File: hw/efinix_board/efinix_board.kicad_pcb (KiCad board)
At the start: 4 copper layers, 62.2 x 56.9 mm, 55 parts, among them U1 T20F256, U2 TPS62826, U3 TPS62826

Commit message: Start working on sdram
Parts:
- added C43: 4.7u, Capacitor_SMD:C_0402_1005Metric, F.Cu at (117.6, 33.2)
- added C44: 0.1u, Capacitor_SMD:C_0201_Small, F.Cu at (105.0, 31.4)
- added C45: 0.1u, Capacitor_SMD:C_0201_Small, F.Cu at (92.0, 33.2)
- added C46: 0.1u, Capacitor_SMD:C_0201_Small, F.Cu at (117.6, 34.2)
- added C47: 4.7u, Capacitor_SMD:C_0402_1005Metric, F.Cu at (117.6, 36.4)
- added C48: 0.1u, Capacitor_SMD:C_0201_Small, F.Cu at (111.8, 46.6)
- added C49: 0.1u, Capacitor_SMD:C_0201_Small, F.Cu at (109.4, 31.4)
- added C50: 0.1u, Capacitor_SMD:C_0201_Small, F.Cu at (113.3, 31.4)
- added C51: 0.1u, Capacitor_SMD:C_0201_Small, F.Cu at (107.0, 46.6)
- added L4: 33 @100MHz, Inductor_SMD:L_0402_1005Metric, F.Cu at (117.6, 35.2)
- added U4: NDS36PT5, Package_SO:TSOP-II-54_22.2x10.16mm_P0.8mm, F.Cu at (104.2, 39.0)
- moved C41 9.18 mm to (67.8, 33.5)
- moved R2 9.18 mm to (74.8, 31.2)
- moved U2 9.18 mm to (77.6, 31.2)
- moved U3 9.18 mm to (66.0, 31.2)
- moved C40 9.18 mm to (62.3, 33.2)
- moved R6 9.18 mm to (63.3, 33.2)
- moved R7 9.18 mm to (64.3, 33.2)
- moved R5 9.18 mm to (63.2, 31.2)
- moved C38 9.18 mm to (79.4, 33.5)
- moved C39 9.18 mm to (79.5, 31.2)
- moved C42 9.18 mm to (67.9, 31.2)
- moved C37 9.18 mm to (73.9, 33.2)
- moved L2 9.18 mm to (82.8, 32.6)
- moved L3 9.18 mm to (71.2, 32.6)
- moved R3 9.18 mm to (74.9, 33.2)
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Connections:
- U1 pad A11: unconnected-(U1-PadA11) -> /fpga/DQ6
- U1 pad A13: unconnected-(U1-PadA13) -> /fpga/DQ3
- U1 pad A14: unconnected-(U1-PadA14) -> /fpga/DQ1
- U1 pad A15: unconnected-(U1-PadA15) -> /fpga/DQ15
- U1 pad B10: unconnected-(U1-PadB10) -> /fpga/DQ7
- U1 pad B11: unconnected-(U1-PadB11) -> /fpga/DQ5
- U1 pad B12: unconnected-(U1-PadB12) -> /fpga/DQ4
- U1 pad B13: unconnected-(U1-PadB13) -> /fpga/DQ2
- U1 pad B14: unconnected-(U1-PadB14) -> /fpga/DQ0
- U1 pad B15: unconnected-(U1-PadB15) -> /fpga/DQ14
- U1 pad B16: unconnected-(U1-PadB16) -> /fpga/DQ13
- U1 pad B9: unconnected-(U1-PadB9) -> /fpga/LQDM
- U1 pad C11: unconnected-(U1-PadC11) -> /fpga/A2
- U1 pad C12: unconnected-(U1-PadC12) -> /fpga/A0
- U1 pad C13: unconnected-(U1-PadC13) -> /fpga/BA1
- U1 pad C14: unconnected-(U1-PadC14) -> /fpga/BA0
- U1 pad C15: unconnected-(U1-PadC15) -> /fpga/DQ12
- U1 pad C16: unconnected-(U1-PadC16) -> /fpga/Q11
- U1 pad D11: unconnected-(U1-PadD11) -> /fpga/A1
- U1 pad D12: unconnected-(U1-PadD12) -> /fpga/A10
- U1 pad D13: unconnected-(U1-PadD13) -> /fpga/~{CS}
- U1 pad D16: unconnected-(U1-PadD16) -> /fpga/DQ10
- U1 pad E11: unconnected-(U1-PadE11) -> /fpga/A3
- U1 pad E12: unconnected-(U1-PadE12) -> /fpga/~{RAS}
- U1 pad E16: unconnected-(U1-PadE16) -> /fpga/DQ9
- U1 pad H12: unconnected-(U1-PadH12) -> /fpga/~{CAS}
- U1 pad J12: unconnected-(U1-PadJ12) -> /fpga/~{WE}
- U1 pad J13: unconnected-(U1-PadJ13) -> /fpga/A4
- U1 pad J14: unconnected-(U1-PadJ14) -> /fpga/A5
- U1 pad J15: unconnected-(U1-PadJ15) -> /fpga/A6
- U1 pad K12: unconnected-(U1-PadK12) -> /fpga/A7
- U1 pad K14: unconnected-(U1-PadK14) -> /fpga/A8
- U1 pad K15: unconnected-(U1-PadK15) -> /fpga/DQ8
- U1 pad K16: unconnected-(U1-PadK16) -> /fpga/UQDM
- U1 pad L15: unconnected-(U1-PadL15) -> /fpga/A9
- U1 pad L16: unconnected-(U1-PadL16) -> /fpga/A11
- U1 pad M15: unconnected-(U1-PadM15) -> /fpga/A12
- U1 pad M16: unconnected-(U1-PadM16) -> /fpga/~{CKE}
- U1 pad P16: unconnected-(U1-PadP16) -> /fpga/CLK
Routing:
- net /fpga/~{WE}: track 0.00 -> 32.1 mm, vias 0 -> 2
- net /fpga/~{CAS}: track 0.00 -> 31.6 mm, vias 0 -> 2
- net /fpga/~{RAS}: track 0.00 -> 27.9 mm, vias 0 -> 2
- net /fpga/~{CS}: track 0.00 -> 25.9 mm, vias 0 -> 2
- net /fpga/A10: track 0.00 -> 24.4 mm, vias 0 -> 2
- net /fpga/A2: track 0.00 -> 24.3 mm, vias 0 -> 2
- net /fpga/A3: track 0.00 -> 24.1 mm, vias 0 -> 2
- net /fpga/A6: track 0.00 -> 24.0 mm, vias 0 -> 2
- net /fpga/BA0: track 0.00 -> 23.8 mm, vias 0 -> 2
- net /fpga/A1: track 0.00 -> 23.8 mm, vias 0 -> 2
- net /fpga/BA1: track 0.00 -> 23.7 mm, vias 0 -> 2
- net /fpga/A4: track 0.00 -> 23.7 mm, vias 0 -> 2
- net /fpga/A7: track 0.00 -> 23.6 mm, vias 0 -> 2
- net /fpga/A5: track 0.00 -> 23.6 mm, vias 0 -> 2
- net /fpga/A8: track 0.00 -> 23.5 mm, vias 0 -> 2
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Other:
- copper layers 4 -> 6

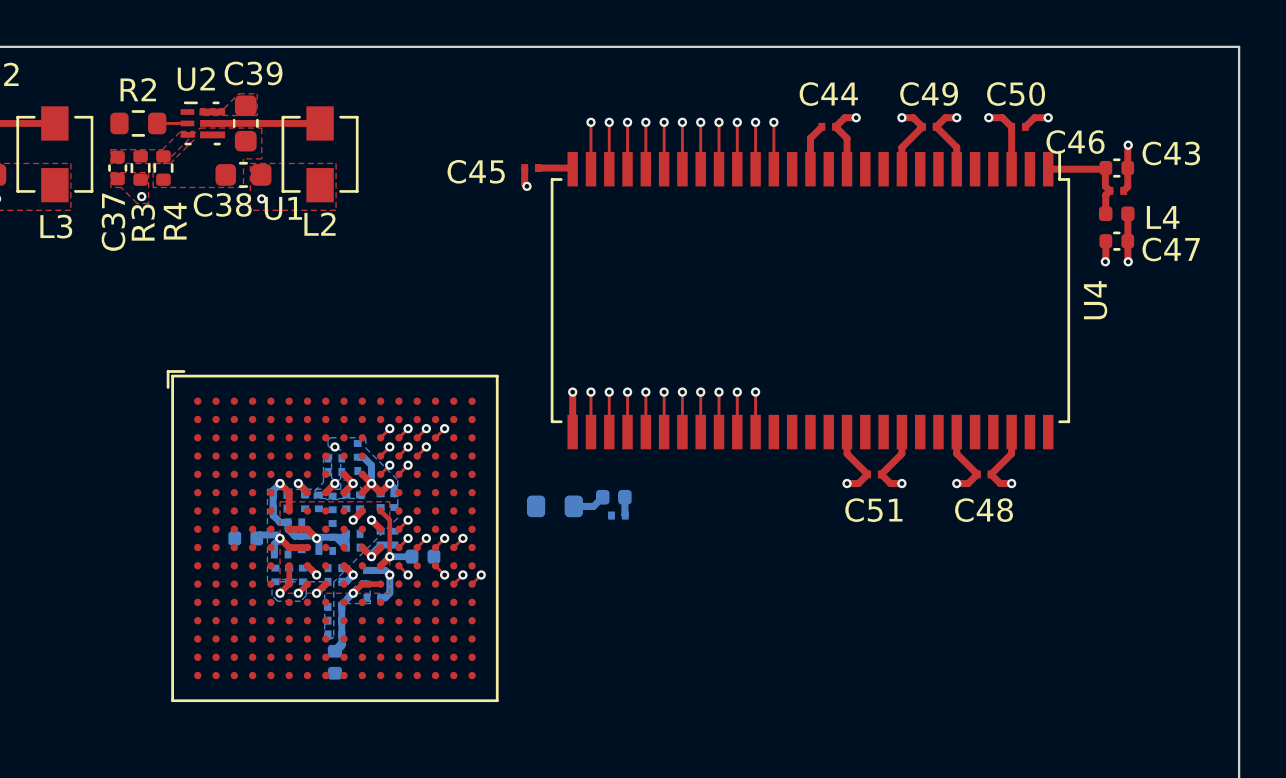
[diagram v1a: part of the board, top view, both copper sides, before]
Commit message: More sdram routing
This changes the pinout from the development board, now DQ8 and UDQM are
different.
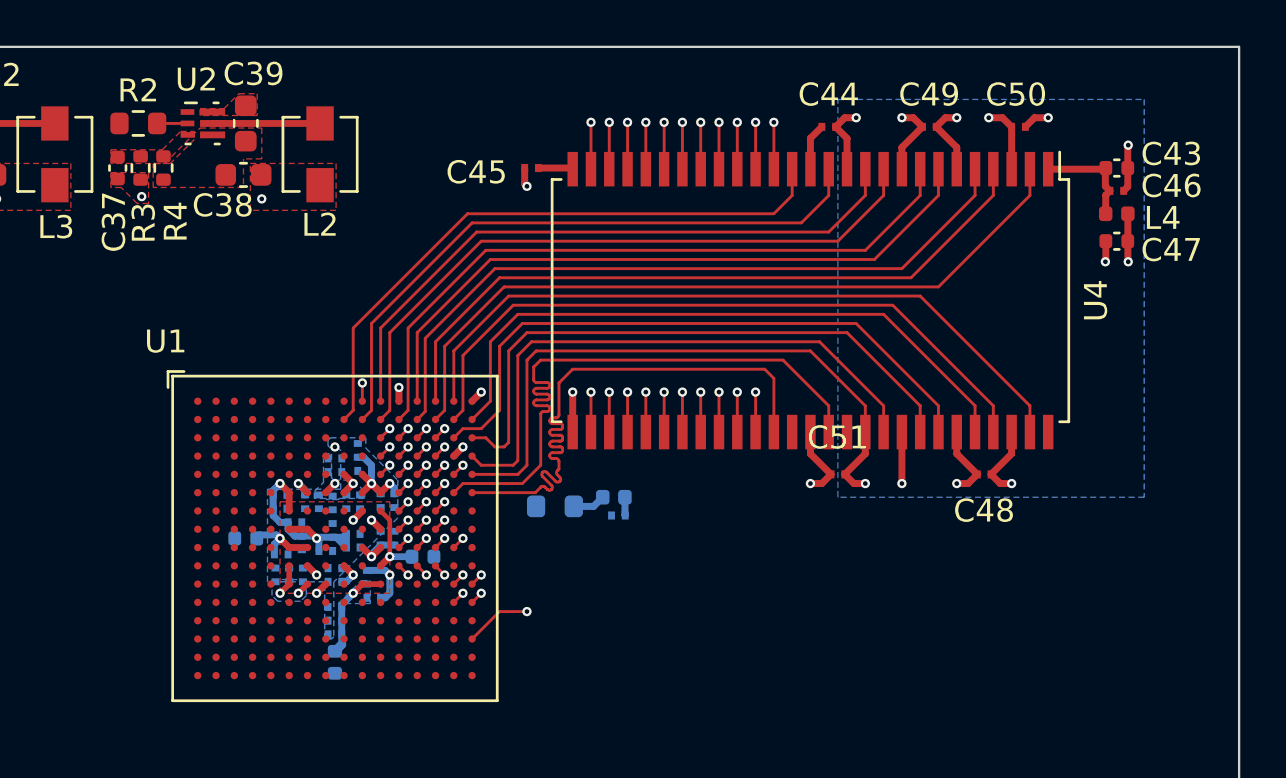
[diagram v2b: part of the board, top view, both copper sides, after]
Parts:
- moved C51 1.60 mm to (105.4, 46.6), turned to 180 degrees
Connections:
- U1 pad C16: /fpga/Q11 -> /fpga/DQ11
- U1 pad F15: unconnected-(U1-PadF15) -> /fpga/DQ8
- U1 pad F16: unconnected-(U1-PadF16) -> /fpga/UQDM
- U1 pad K15: /fpga/DQ8 -> unconnected-(U1-PadK15)
- U1 pad K16: /fpga/UQDM -> unconnected-(U1-PadK16)
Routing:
- net /fpga/DQ0: track 0.00 -> 32.8 mm
- net /fpga/DQ15: track 0.00 -> 31.5 mm
- net /fpga/DQ2: track 0.00 -> 31.5 mm
- net /fpga/DQ1: track 0.00 -> 30.8 mm
- net /fpga/DQ4: track 0.00 -> 30.1 mm
- net /fpga/DQ14: track 0.00 -> 30.0 mm
- net /fpga/DQ3: track 0.00 -> 29.4 mm
- net /fpga/DQ5: track 0.00 -> 29.2 mm
- net /fpga/DQ13: track 0.00 -> 28.2 mm
- net /fpga/DQ6: track 0.00 -> 28.0 mm
- net /fpga/DQ7: track 0.00 -> 27.8 mm
- net /fpga/DQ9: track 0.00 -> 27.6 mm, vias 0 -> 1
- net /fpga/DQ12: track 0.00 -> 27.6 mm
- net /fpga/LQDM: track 0.00 -> 26.9 mm
- net /fpga/DQ8: track 0.00 -> 26.9 mm
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- added copper zone on B.Cu, net VCCQ

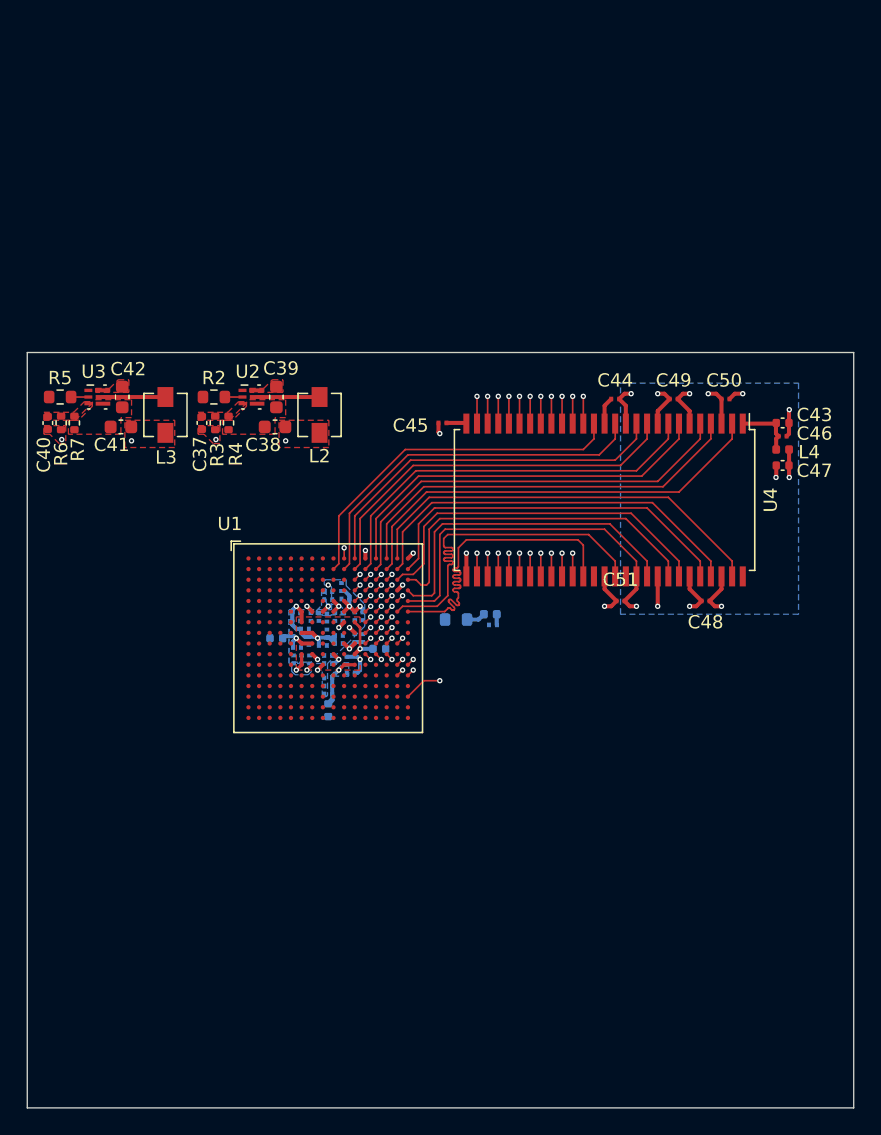
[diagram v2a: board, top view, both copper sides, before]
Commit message: Add CPU and begin sch/layout
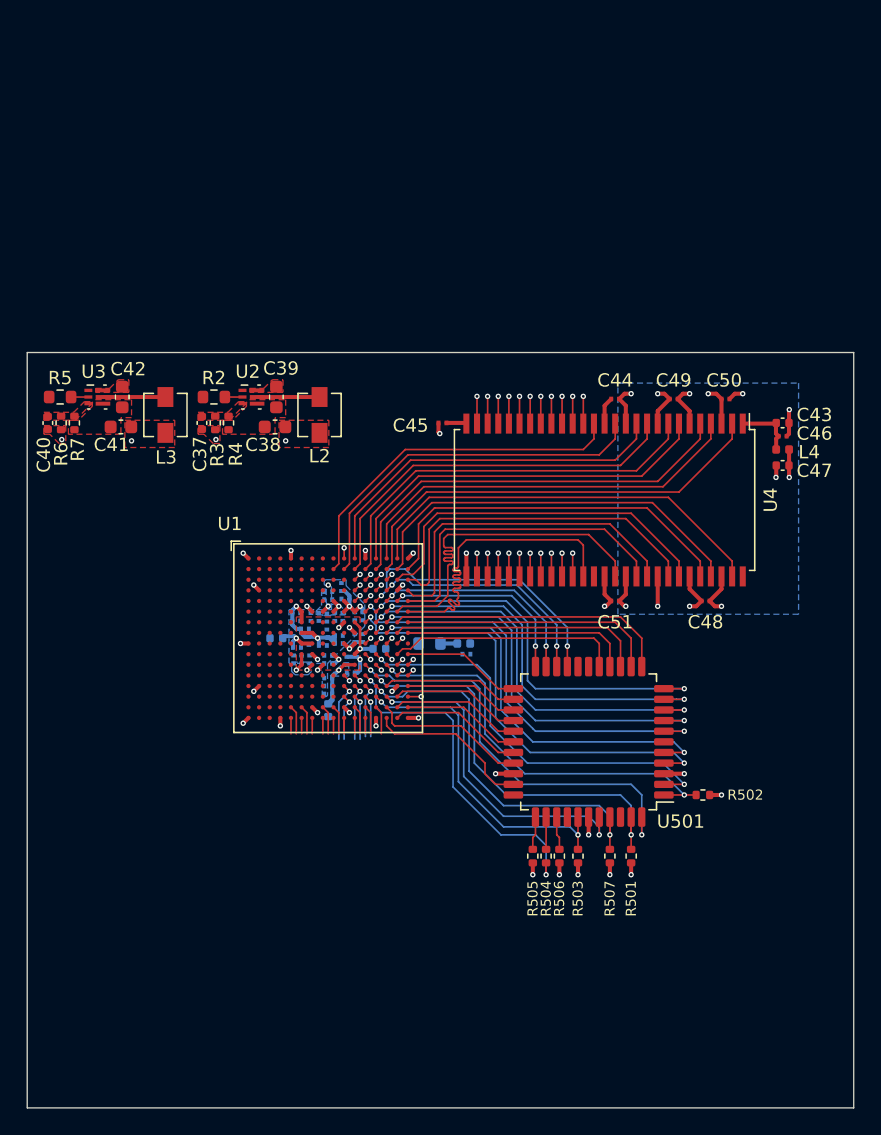
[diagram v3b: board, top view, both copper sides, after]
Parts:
- added R501: 10k, Resistor_SMD:R_0402_1005Metric, F.Cu at (106.2, 65.8)
- added R502: 10k, Resistor_SMD:R_0402_1005Metric, F.Cu at (111.6, 61.2)
- added R503: 10k, Resistor_SMD:R_0402_1005Metric, F.Cu at (102.2, 65.8)
- added R504: 0R, Resistor_SMD:R_0402_1005Metric, F.Cu at (99.8, 65.8)
- added R505: 10k, Resistor_SMD:R_0402_1005Metric, F.Cu at (98.8, 65.8)
- added R506: 10k, Resistor_SMD:R_0402_1005Metric, F.Cu at (100.8, 65.8)
- added R507: 10k, Resistor_SMD:R_0402_1005Metric, F.Cu at (104.6, 65.8)
- added U501: W65C02SQ, Package_QFP:LQFP-44_10x10mm_P0.8mm, F.Cu at (103.0, 57.2)
- moved C1 2.97 mm to (93.8, 50.6)
- moved L1 2.97 mm to (93.6, 49.8)
- moved R1 2.69 mm to (91.0, 49.8)
- moved C51 0.40 mm to (105.0, 46.6)
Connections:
- U1 pad D14: unconnected-(U1-PadD14) -> /cpu/CPU_A13
- U1 pad E13: unconnected-(U1-PadE13) -> /cpu/CPU_A12
- U1 pad E14: unconnected-(U1-PadE14) -> /cpu/CPU_A14
- U1 pad E15: unconnected-(U1-PadE15) -> /cpu/CPU_A15
- U1 pad F12: unconnected-(U1-PadF12) -> /cpu/CPU_A2
- U1 pad F13: unconnected-(U1-PadF13) -> /cpu/CPU_A6
- U1 pad F14: unconnected-(U1-PadF14) -> /cpu/CPU_A5
- U1 pad G12: unconnected-(U1-PadG12) -> /cpu/CPU_A0
- U1 pad G13: unconnected-(U1-PadG13) -> /cpu/CPU_A4
- U1 pad G14: unconnected-(U1-PadG14) -> /cpu/CPU_A3
- U1 pad G15: unconnected-(U1-PadG15) -> /cpu/CPU_A7
- U1 pad G16: unconnected-(U1-PadG16) -> /cpu/CPU_A8
- U1 pad H13: unconnected-(U1-PadH13) -> /fpga/CLK_50
- U1 pad H14: unconnected-(U1-PadH14) -> /cpu/CPU_A1
- U1 pad H15: unconnected-(U1-PadH15) -> /cpu/CPU_A9
- U1 pad H16: unconnected-(U1-PadH16) -> /cpu/CPU_A10
- U1 pad K13: unconnected-(U1-PadK13) -> /cpu/CPU_SYNC
- U1 pad K15: unconnected-(U1-PadK15) -> /cpu/CPU_A11
- U1 pad K16: unconnected-(U1-PadK16) -> /cpu/CPU_D7
- U1 pad L12: unconnected-(U1-PadL12) -> /cpu/CPU_~{MLB}
- U1 pad L13: unconnected-(U1-PadL13) -> /fpga/CLK_50
- U1 pad L14: unconnected-(U1-PadL14) -> /cpu/CPU_~{NMIB}
- U1 pad M12: unconnected-(U1-PadM12) -> /cpu/CPU_PHI2
- U1 pad M13: unconnected-(U1-PadM13) -> /cpu/CPU_~{IRQB}
- U1 pad N13: unconnected-(U1-PadN13) -> /cpu/CPU_RDY
- U1 pad N14: unconnected-(U1-PadN14) -> /cpu/CPU_D6
- U1 pad N16: unconnected-(U1-PadN16) -> /cpu/CPU_D5
- U1 pad P13: unconnected-(U1-PadP13) -> /cpu/CPU_~{RESB}
- U1 pad P14: unconnected-(U1-PadP14) -> /cpu/CPU_~{VPB}
- U1 pad P15: unconnected-(U1-PadP15) -> /cpu/CPU_D4
- U1 pad R14: unconnected-(U1-PadR14) -> /cpu/CPU_D0
- U1 pad R15: unconnected-(U1-PadR15) -> /cpu/CPU_D3
- U1 pad R16: unconnected-(U1-PadR16) -> /cpu/CPU_D2
- U1 pad T14: unconnected-(U1-PadT14) -> /cpu/CPU_~{RWB}
- U1 pad T15: unconnected-(U1-PadT15) -> /cpu/CPU_D1
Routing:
- net /cpu/CPU_A0: track 0.00 -> 34.0 mm, vias 0 -> 2
- net /cpu/CPU_A2: track 0.00 -> 32.9 mm, vias 0 -> 2
- net /cpu/CPU_~{MLB}: track 0.00 -> 31.5 mm, vias 0 -> 2
- net /cpu/CPU_A1: track 0.00 -> 31.2 mm, vias 0 -> 2
- net /cpu/CPU_~{NMIB}: track 0.00 -> 31.1 mm, vias 0 -> 2
- net /cpu/CPU_A4: track 0.00 -> 31.0 mm, vias 0 -> 2
- net /cpu/CPU_~{IRQB}: track 0.00 -> 30.9 mm, vias 0 -> 2
- net /cpu/CPU_SYNC: track 0.00 -> 30.9 mm, vias 0 -> 2
- net /cpu/CPU_A6: track 0.00 -> 30.4 mm, vias 0 -> 2
- net /cpu/CPU_A3: track 0.00 -> 30.3 mm, vias 0 -> 2
- net /cpu/CPU_A5: track 0.00 -> 29.7 mm, vias 0 -> 2
- net /cpu/CPU_RDY: track 0.00 -> 29.0 mm, vias 0 -> 2
- net /cpu/CPU_PHI2: track 0.00 -> 25.9 mm, vias 0 -> 2
- net /cpu/CPU_~{VPB}: track 0.00 -> 24.9 mm, vias 0 -> 2
- net /cpu/CPU_~{RESB}: track 0.00 -> 24.9 mm, vias 0 -> 2
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- added copper zone on In1.Cu, net (none)
- removed copper zone on In1.Cu, net Net-(C2-Pad1)

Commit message: More routing
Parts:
- moved C3 0.30 mm to (87.5, 50.4)
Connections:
- U501 pad 6: unconnected-(U501-Pad33) -> unconnected-(U501-Pad6)
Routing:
- net /fpga/A8: track 23.5 -> 15.2 mm
- net GND: track 36.3 -> 42.5 mm, vias 32 -> 36
- net Net-(C2-Pad1): track 4.89 -> 8.65 mm
- net +1V2: track 12.1 -> 13.7 mm, vias 6 -> 7
- added copper zone on In2.Cu, net +1V2
- added copper zone on In4.Cu, net GND

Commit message: Update schematics and board
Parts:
- added R10: 100k, Resistor_SMD:R_0402_1005Metric, F.Cu at (103.9, 10.6)
- added R8: 100k, Resistor_SMD:R_0402_1005Metric, F.Cu at (101.0, 10.6)
- added R9: 33R, Resistor_SMD:R_0402_1005Metric, F.Cu at (101.0, 12.6)
- added SW1: SW_Push, Button_Switch_THT:SW_1825966-1, F.Cu at (104.6, 7.11)
- added U5: ADM6713, Package_SC:ADM6711TAKSZ-REEL7, F.Cu at (93.7, 11.8)
- added U6: FT2232HL, Package_QFP:LQFP-64_10x10mm_P0.5mm, F.Cu at (70.2, 11.8)
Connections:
- U1 pad K6: +3V3 -> unconnected-(U1-PadK6)
